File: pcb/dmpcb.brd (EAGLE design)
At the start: 100 x 100 mm, 44 parts, among them IC1 7805DT, IC2 L293D, IC3 MAX7219CNG, Q1 IRF530, Q2 IRF530

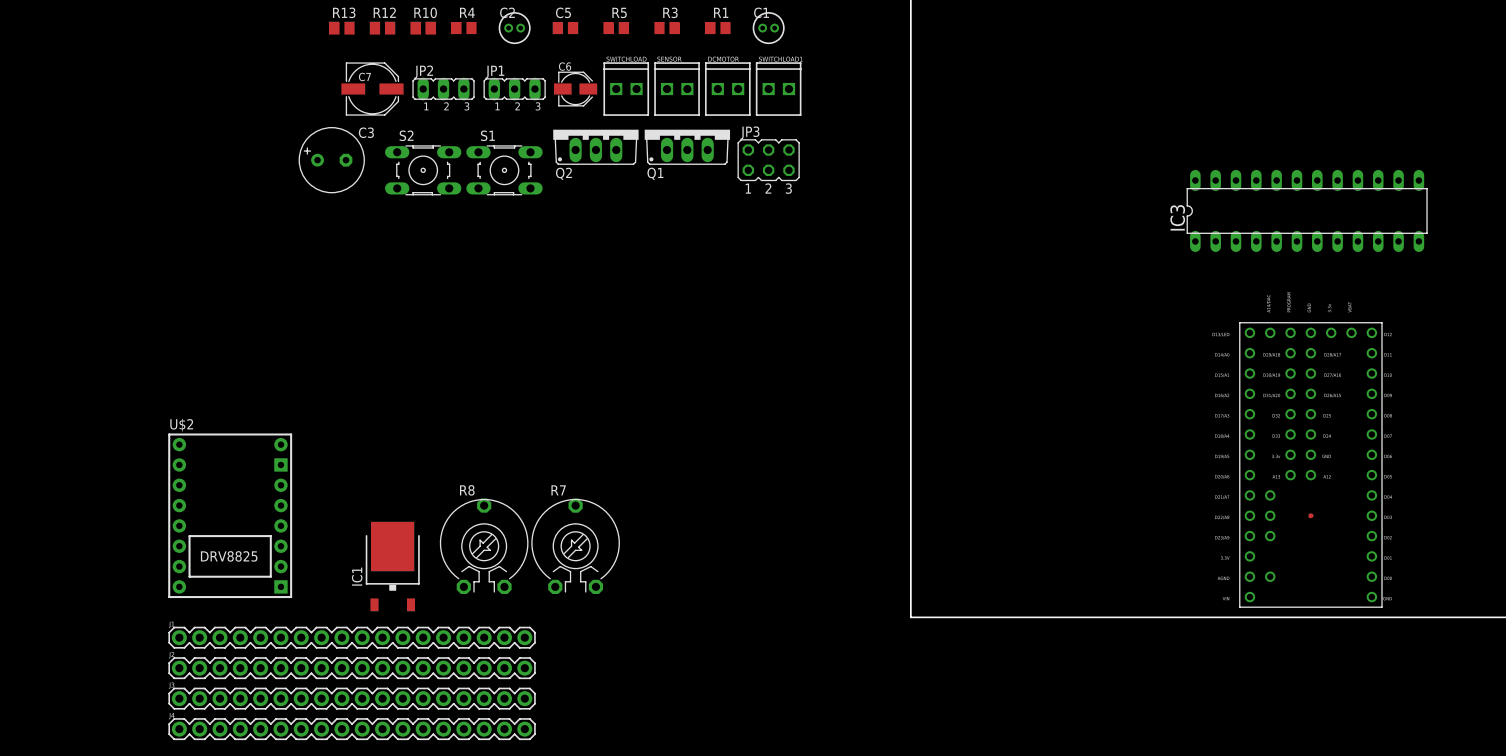
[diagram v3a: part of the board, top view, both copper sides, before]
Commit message: added other teensy lib, has better pin spacing, also added breakout jumpers for all pins (-RX and TX)
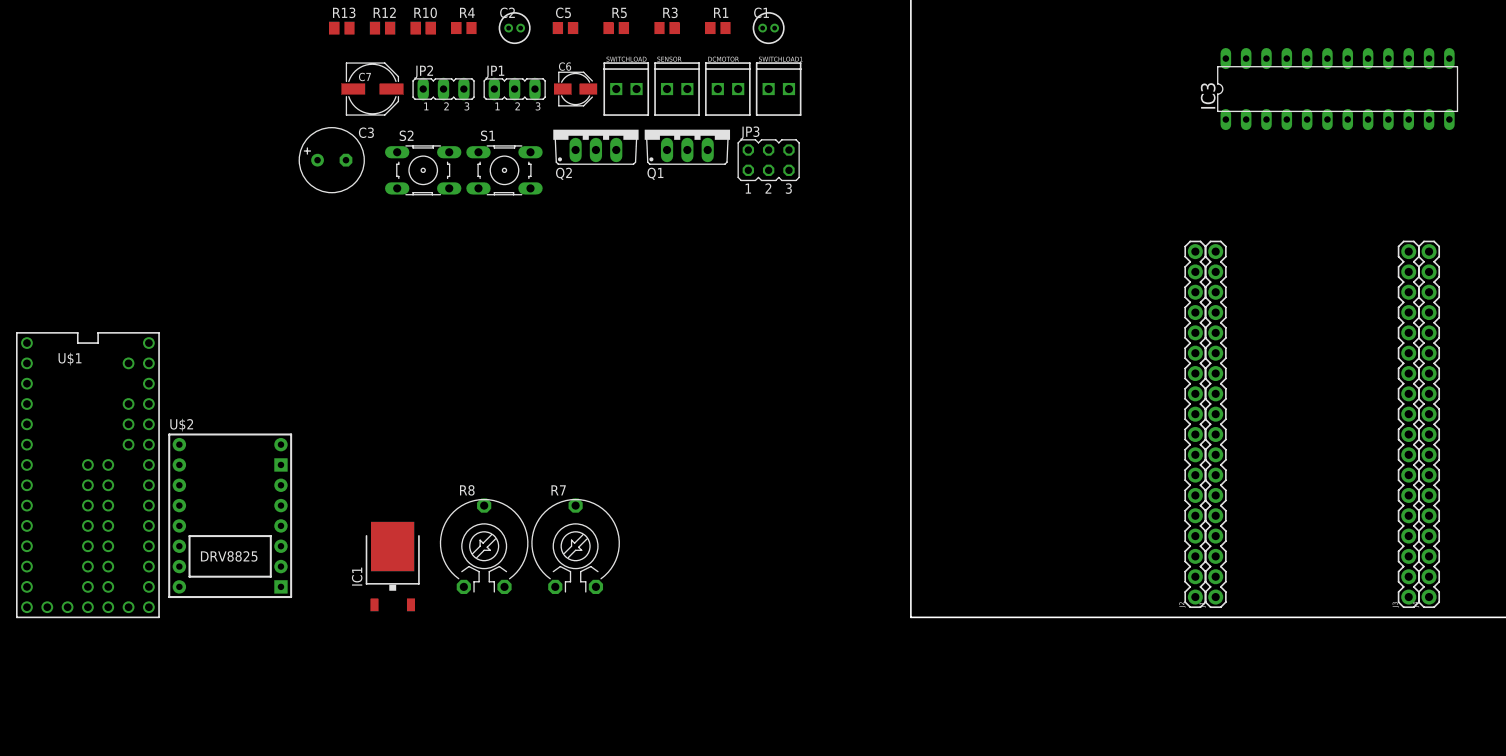
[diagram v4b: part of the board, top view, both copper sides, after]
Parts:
- U$1: value TEENSY3.1_ALL -> TEENSY_3.1-3.2_ALL_PINS&PADS; device Teensy3.1_ralfsfix:TEENSY3.1_ALL_RALF -> Teensy_3_and_LC_Series_Boards_v1.4:TEENSY_3.0-3.2_ALL_PINS_&_PADS
- moved J4 157.1 mm to (64.8, 2.54), turned to 90 degrees
- moved J3 154.2 mm to (62.2, 2.54), turned to 90 degrees
- moved U$1 147.9 mm to (-102.9, 17.8), turned to 0 degrees
- moved J1 129.6 mm to (38.1, 2.54), turned to 90 degrees
- moved J2 127.3 mm to (35.6, 2.54), turned to 90 degrees
- moved IC3 15.7 mm to (53.3, 66.0)
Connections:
- removed net AUDIOOUT: U$1.A14/DAC
- removed net POT1: U$1.D22/A8
- removed net POT2: U$1.D18/A4
- new net AGND: U$1.AGND
- new net AREF: U$1.AREF
- new net N$22: J2.1, U$1.24
- new net N$23: J2.2, U$1.23/A9
- new net N$26: J2.3, U$1.22/A8
- new net N$27: J2.4, U$1.21/A7
- new net N$28: J2.5, U$1.20/A6
- new net N$30: J2.7, U$1.18/A4
- new net N$31: J2.8, U$1.17/A3
- new net N$36: J2.13, U$1.12
- new net N$37: J2.14, U$1.11
- new net N$38: J2.15, U$1.10
- new net N$39: J2.16, U$1.9
- new net N$40: J2.17, U$1.8
- new net N$41: J2.18, U$1.7
- new net N$42: J3.18, U$1.25
- new net N$43: J3.17, U$1.26
- new net N$44: J3.16, U$1.27
- new net N$45: J3.15, U$1.28
- new net N$46: J3.14, U$1.29
- new net N$47: J3.13, U$1.30
- new net N$48: J3.12, U$1.31
- new net N$49: J3.11, U$1.32
- new net N$50: J3.10, U$1.33
- new net N$51: J3.9, U$1.A10
- new net N$52: J3.8, U$1.A11
- new net N$53: J3.7, U$1.A12
- new net N$54: J3.6, U$1.A13
- new net N$55: J3.5, U$1.RESET/DAC
- new net N$61: U$1.1
- new net N$62: U$1.0
- new net PIN2: U$1.2
- new net PIN3: J3.1, U$1.3
- new net PIN4: J3.2, U$1.4
- new net PIN5: J3.3, U$1.5
- new net PIN6: J3.4, U$1.6
- new net VBAT: U$1.VBAT
- new net VUSB: U$1.VUSB
- net 3.3V: now also U$1.3.3V, U$1.3.3V1, U$1.3.3V2; no longer U$1.3.3V@1, U$1.3.3V@2, U$1.3.3V@3
- net BUTTON01: no longer U$1.D4
- net BUTTON02: no longer U$1.D5
- net GND: now also U$1.GND, U$1.GND1, U$1.GND2; no longer U$1.GND@1, U$1.GND@2, U$1.GND@3
- net L293EN: no longer U$1.D8
- net L293IN01: no longer U$1.D6
- net L293IN02: no longer U$1.D7
- net MAX7219CLK: no longer U$1.D12
- net MAX7219DIN: no longer U$1.D10
- net MAX7219LOAD: no longer U$1.D11
- net MOSFET01: no longer U$1.D2
- net MOSFET02: no longer U$1.D3
- net N$29: now also J2.6, U$1.19/A5; no longer U$1.D0
- net N$32: now also J2.9, U$1.16/A2; no longer U$1.D23/A9
- net N$33: now also J2.10, U$1.15/A1; no longer U$1.D21/A7
- net N$34: now also J2.11, U$1.14/A0; no longer U$1.D19/A5
- net N$35: now also J2.12, U$1.13; no longer U$1.D20/A6
- net POT01: no longer U$1.A11
- net POT02: no longer U$1.A10
- net SENSORPORT: no longer U$1.D9

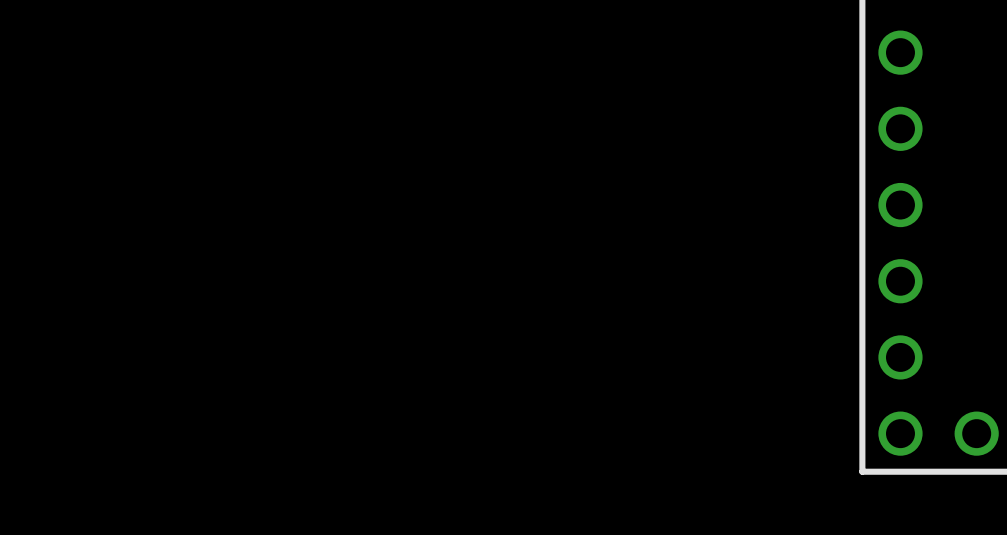
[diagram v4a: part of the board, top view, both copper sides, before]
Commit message: fixed drv8825, also added lm358
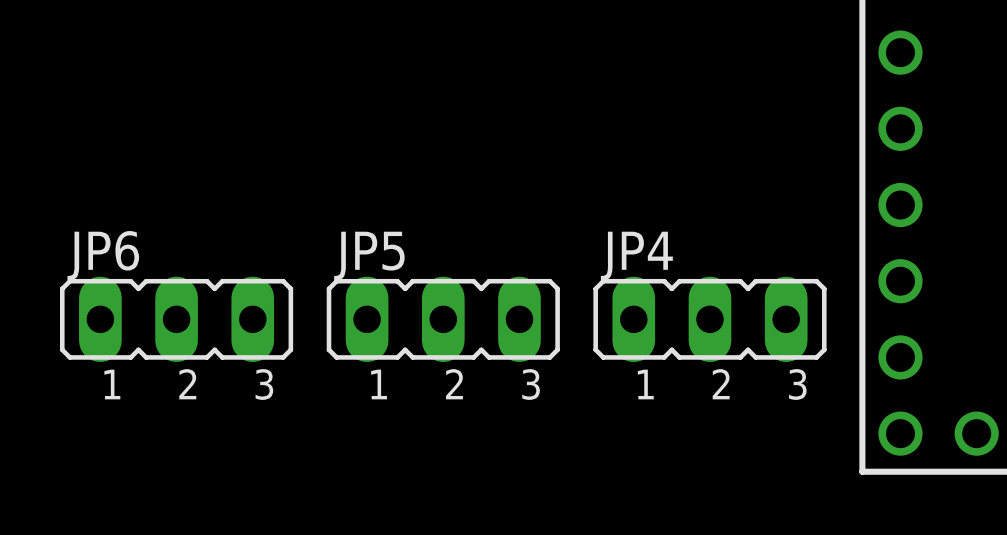
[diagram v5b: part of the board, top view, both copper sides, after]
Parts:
- added JP4, JP5, JP6: (no value), jumper:JP2
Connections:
- removed net DIR: U$2.DIR
- removed net EN: U$2.EN_N
- removed net L293EN: IC2.1
- removed net L293IN01: IC2.2
- removed net L293IN02: IC2.7
- removed net M0: U$2.M0
- removed net M1: U$2.M1
- removed net M2: U$2.M2
- removed net RST: U$2.RST_N
- removed net SLP: U$2.SLP_N
- removed net STP: U$2.STEP_N
- new net DRV8825DIR: J1.10, U$2.DIR
- new net DRV8825EN: J1.9, U$2.EN_N
- new net DRV8825RST: J1.12, U$2.RST_N
- new net DRV8825SLP: J1.13, U$2.SLP_N
- new net DRV8825STEP: J1.11, U$2.STEP_N
- new net LM293EN: IC2.1, J1.3
- new net LM293IN01: IC2.2, J1.4
- new net LM293IN02: IC2.7, J1.5
- new net N$56: J4.17
- new net N$57: JP4.2, U$2.M2
- new net N$58: JP5.2, U$2.M1
- new net N$59: JP6.2, U$2.M0
- new net N$64: J1.14
- net +5V: now also JP4.3, JP5.3, JP6.3
- net BUTTON01: now also J1.1
- net BUTTON02: now also J1.2
- net GND: now also JP4.1, JP5.1, JP6.1
- net MAX7219CLK: now also J1.7
- net MAX7219DIN: now also J1.6
- net MAX7219LOAD: now also J1.8
- net MOSFET01: now also J4.16
- net MOSFET02: now also J4.15
- net POT01: now also J4.13
- net POT02: now also J4.12
- net SENSORPORT: now also J4.18

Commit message: need to add custom component for dotmatrix display
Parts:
- added IC4: LM358D, linear:SO08
- added R15, R16: 10K, rcl:M0805
- moved U$1 152.7 mm to (49.8, 19.1), turned to 180 degrees
- moved SWITCHLOAD 133.5 mm to (96.5, 59.7), turned to 270 degrees
- moved SENSOR 127.6 mm to (96.5, 53.3), turned to 270 degrees
- moved DCMOTOR 122.1 mm to (96.5, 47.0), turned to 270 degrees
- moved SWITCHLOAD1 117.1 mm to (96.5, 40.6), turned to 270 degrees
- moved U$2 109.2 mm to (24.1, 11.4), turned to 180 degrees
- moved C7 99.6 mm to (11.4, 5.08), turned to 270 degrees
- moved IC3 94.9 mm to (-38.1, 40.6)
- moved J1 1.27 mm to (36.8, 2.54)
- moved J2 1.27 mm to (34.3, 2.54)
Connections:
- new net N$65: IC4.2, R15.2, R16.1
- new net OPAMPIN: IC4.3
- new net OPAMPOUT: IC4.1, J4.10, R15.1
- net +5V: now also IC4.8
- net GND: now also IC4.4, R16.2
- net SENSORPORT: now also J4.11

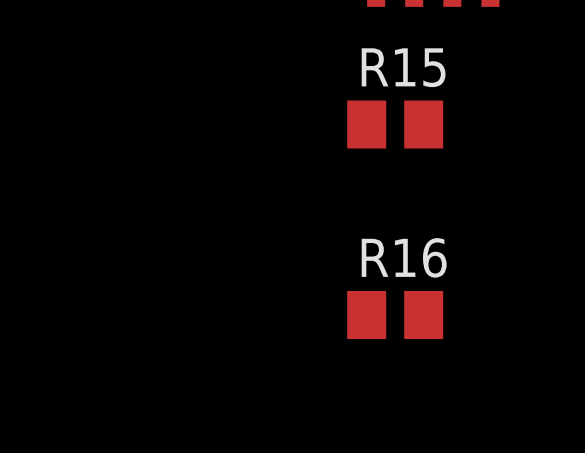
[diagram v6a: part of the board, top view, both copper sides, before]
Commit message: added jumper around 7805, if 5v load is bigger than 1Amp
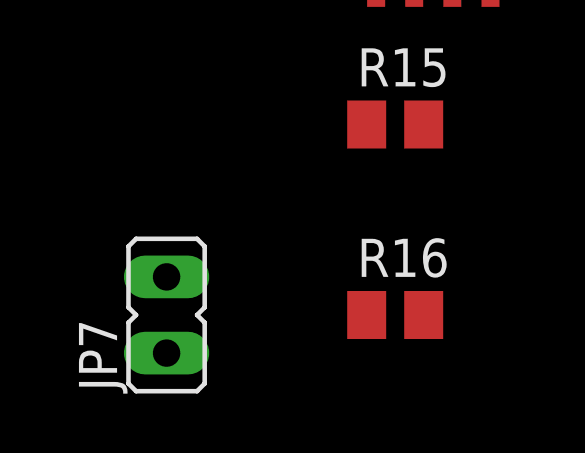
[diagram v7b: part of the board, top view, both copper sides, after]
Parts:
- added JP7: (no value), jumper:JP1
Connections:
- net +5V: now also JP7.2
- net V+: now also JP7.1
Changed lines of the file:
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@@
 <attribute name="VALUE" x="-146.05" y="-12.7" size="1.27" layer="27"/>
+</element>
+<element name="JP7" library="jumper" library_urn="urn:adsk.eagle:library:252" package="JP1" package3d_urn="urn:adsk.eagle:package:15455/1" value="" x="-152.4" y="-10.16" smashed="yes">
+<attribute name="NAME" x="-154.051" y="-12.7" size="1.27" layer="25" ratio="10" rot="R90"/>
+<attribute name="VALUE" x="-149.479" y="-12.7" size="1.27" layer="27" ratio="10" rot="R90"/>
 </element>
 </elements>
@@
 <contactref element="JP2" pad="1"/>
 <contactref element="IC2" pad="8"/>
-<wire x1="96.52" y1="40.64" x2="91.44" y2="35.56" width="0" layer="19" extent="1-1"/>
-<wire x1="-17.03" y1="73.66" x2="96.52" y2="40.64" width="0" layer="19" extent="1-1"/>
-<wire x1="96.52" y1="59.69" x2="96.52" y2="40.64" width="0" layer="19" extent="1-1"/>
-<wire x1="-52.07" y1="66.04" x2="96.52" y2="59.69" width="0" layer="19" extent="1-1"/>
-<wire x1="-60.96" y1="66.04" x2="-52.07" y2="66.04" width="0" layer="19" extent="1-1"/>
+<contactref element="JP7" pad="1"/>
+<wire x1="-67.05" y1="1.55" x2="-152.4" y2="-11.43" width="0" layer="19" extent="1-1"/>
+<wire x1="-74.168" y1="57.15" x2="-67.05" y2="1.55" width="0" layer="19" extent="1-1"/>
+<wire x1="-60.96" y1="66.04" x2="-74.168" y2="57.15" width="0" layer="19" extent="1-1"/>
+<wire x1="-52.07" y1="66.04" x2="-60.96" y2="66.04" width="0" layer="19" extent="1-1"/>
 <wire x1="-49.276" y1="80.01" x2="-52.07" y2="66.04" width="0" layer="19" extent="1-1"/>
 <wire x1="-45.72" y1="80.01" x2="-49.276" y2="80.01" width="0" layer="19" extent="1-1"/>
 <wire x1="-55.626" y1="80.01" x2="-49.276" y2="80.01" width="0" layer="19" extent="1-1"/>
-<wire x1="-74.168" y1="57.15" x2="-60.96" y2="66.04" width="0" layer="19" extent="1-1"/>
-<wire x1="-67.05" y1="1.55" x2="-74.168" y2="57.15" width="0" layer="19" extent="1-1"/>
+<wire x1="-17.03" y1="73.66" x2="-45.72" y2="80.01" width="0" layer="19" extent="1-1"/>
+<wire x1="96.52" y1="59.69" x2="-17.03" y2="73.66" width="0" layer="19" extent="1-1"/>
+<wire x1="96.52" y1="40.64" x2="96.52" y2="59.69" width="0" layer="19" extent="1-1"/>
+<wire x1="91.44" y1="35.56" x2="96.52" y2="40.64" width="0" layer="19" extent="1-1"/>
 </signal>
 <signal name="+5V">
@@
 <contactref element="JP6" pad="3"/>
 <contactref element="IC4" pad="8"/>
+<contactref element="JP7" pad="2"/>
+<wire x1="-145.415" y1="6.41" x2="-152.4" y2="-8.89" width="0" layer="19" extent="1-1"/>
 <wire x1="-132.08" y1="5.08" x2="-145.415" y2="6.41" width="0" layer="19" extent="1-1"/>
 <wire x1="-123.19" y1="5.08" x2="-132.08" y2="5.08" width="0" layer="19" extent="1-1"/>
 <wire x1="-114.3" y1="5.08" x2="-123.19" y2="5.08" width="0" layer="19" extent="1-1"/>
-<wire x1="42.18" y1="2.54" x2="-114.3" y2="5.08" width="0" layer="19" extent="1-1"/>
-<wire x1="-62.49" y1="1.55" x2="42.18" y2="2.54" width="0" layer="19" extent="1-1"/>
-<wire x1="-62.45" y1="78.74" x2="42.18" y2="2.54" width="0" layer="19" extent="1-1"/>
-<wire x1="-48.78" y1="73.66" x2="-62.45" y2="78.74" width="0" layer="19" extent="1-1"/>
-<wire x1="-44.13" y1="73.66" x2="-48.78" y2="73.66" width="0" layer="19" extent="1-1"/>
-<wire x1="-40.31" y1="66.04" x2="-44.13" y2="73.66" width="0" layer="19" extent="1-1"/>
+<wire x1="-62.49" y1="1.55" x2="-114.3" y2="5.08" width="0" layer="19" extent="1-1"/>
+<wire x1="-39.37" y1="44.45" x2="-62.49" y2="1.55" width="0" layer="19" extent="1-1"/>
+<wire x1="-40.31" y1="66.04" x2="-39.37" y2="44.45" width="0" layer="19" extent="1-1"/>
+<wire x1="-44.13" y1="73.66" x2="-40.31" y2="66.04" width="0" layer="19" extent="1-1"/>
+<wire x1="-48.78" y1="73.66" x2="-44.13" y2="73.66" width="0" layer="19" extent="1-1"/>
+<wire x1="-62.45" y1="78.74" x2="-48.78" y2="73.66" width="0" layer="19" extent="1-1"/>
 <wire x1="-14.29" y1="80.01" x2="-40.31" y2="66.04" width="0" layer="19" extent="1-1"/>
-<wire x1="-39.37" y1="44.45" x2="-14.29" y2="80.01" width="0" layer="19" extent="1-1"/>
-<wire x1="83.82" y1="17.78" x2="-39.37" y2="44.45" width="0" layer="19" extent="1-1"/>
+<wire x1="42.18" y1="2.54" x2="-39.37" y2="44.45" width="0" layer="19" extent="1-1"/>
+<wire x1="83.82" y1="17.78" x2="42.18" y2="2.54" width="0" layer="19" extent="1-1"/>
 </signal>
 <signal name="G">

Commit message: added felix' better audio output (thank you felix). still need to find use for one half opamp. Ideas?
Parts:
- added C4: 100nf, rcl:C0805
- added C8, C9: 100uf, rcl:PANASONIC_B
- added IC5: LM358D, linear:SO08
- added J5, J6: (no value), SparkFun-Connectors:1X05
- added J7: SJ-3523-SMT-TR, SJ-3523-SMT-TR:CUI_SJ-3523-SMT-TR
- added R17, R19: b10k, pot:RJ9W
- added R18: 270R, rcl:M0805
- added R20: 10K, rcl:M0805
- added R21: b100k, pot:RJ9W
- R15: value 10K -> b100k; device rcl:M0805 -> pot:RJ9W
- moved IC4 182.5 mm to (6.35, 108.0)
- moved JP7 164.7 mm to (11.4, 6.35)
- moved R7 149.4 mm to (85.1, 87.6)
- moved JP4 135.8 mm to (-52.1, 124.5), turned to 270 degrees
- moved C7 130.8 mm to (-66.0, 110.5)
- moved S1 127.2 mm to (72.4, 87.6), turned to 90 degrees
- moved R8 102.8 mm to (12.7, 87.6)
- moved R16 96.6 mm to (-59.7, 35.6)
- moved C3 93.2 mm to (11.4, 16.5)
- moved S2 92.0 mm to (25.4, 87.6), turned to 90 degrees
- moved IC1 87.7 mm to (22.9, 10.2)
- moved U$2 75.5 mm to (80.0, 62.2)
- moved JP6 70.1 mm to (-82.5, 52.1)
- moved R15 63.5 mm to (-81.3, -5.08)
- moved JP5 58.9 mm to (-78.7, 40.6)
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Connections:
- removed net N$65: IC4.2, R15.2, R16.1
- new net BETTERAUDIOOUT: J4.14, R17.E
- new net N$63: IC4.2, R15.A, R16.1
- new net N$66: C8.+, J7.2
- new net N$67: R17.A, R17.S, R18.2
- new net N$68: C4.1, IC5.3, R18.1
- new net N$69: IC5.1, IC5.2, R19.E
- new net N$71: IC5.5, R19.S
- new net N$72: C8.-, C9.-, IC5.6, IC5.7
- new net N$73: C9.+, J7.3
- new net N$75: IC4.6, R20.1, R21.A
- net +5V: now also IC5.8, J5.5
- net GND: now also C4.2, IC5.4, J5.4, J6.1, J6.2, J6.3, J6.4, J6.5, J7.1, R19.A, R20.2
- net MAX7219CLK: now also J5.1
- net MAX7219DIN: now also J5.3
- net MAX7219LOAD: now also J5.2
- net OPAMPIN: now also IC4.5
- net OPAMPOUT: now also IC4.7, R15.E, R15.S, R21.E, R21.S; no longer R15.1
